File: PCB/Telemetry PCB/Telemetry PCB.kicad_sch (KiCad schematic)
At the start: 36 parts, among them IC1 E22-900M22S, J1 Conn_01x04_Pin, J2 GPS, J3 Batt, SW1 SW_MEC_5E, SW2 SW_MEC_5E, U1 STM32F411CEUx, U2 AP62200WU, Y1 25MHZ 9pF, Y2 32.768k 6pF

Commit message: added footprints
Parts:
- removed C15: 100-330nF, symbol Device:C
- removed L1: 1kohm 100MHz, symbol Device:L
- added C15: 1F, Capacitor_THT:C_Radial_D10.0mm_H20.0mm_P5.00mm, symbol Device:C_Polarized
- C1, C10, C11, C12, C13, C16, C17, C2, C3, C4, C5, C6, C7, C8, C9: footprint (none) -> Capacitor_SMD:C_1206_3216Metric_Pad1.33x1.80mm_HandSolder
- C14: value C -> 100nF; footprint (none) -> Capacitor_SMD:C_1206_3216Metric_Pad1.33x1.80mm_HandSolder
- J1, J2: footprint (none) -> Connector_PinHeader_2.54mm:PinHeader_1x04_P2.54mm_Vertical
- J3: footprint (none) -> Connector_PinHeader_2.54mm:PinHeader_1x02_P2.54mm_Vertical
- R1, R2, R3, R4, R5, R6: footprint (none) -> Resistor_SMD:R_1206_3216Metric_Pad1.30x1.75mm_HandSolder
- SW1, SW2: footprint (none) -> Button_Switch_SMD:SW_Push_1P1T_NO_6x6mm_H9.5mm
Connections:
- net +3.3V: now also C15.1
- net GND: now also C15.2
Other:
- note added: "Voltage Stabilization"

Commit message: more footprints
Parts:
- added J4: Serial Debug Header 1x4, Connector_PinHeader_2.54mm:PinHeader_1x04_P2.54mm_Vertical, symbol Connector_Generic:Conn_01x04
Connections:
- net +3.3V: now also J4.3 (Pin_3)
- net GND: now also J4.4 (Pin_4)
- net TX2: now reaches U1.12 (PA2)
- net TX2: now also J4.2 (Pin_2)
- net RX2: now reaches U1.13 (PA3)
- net RX2: now also J4.1 (Pin_1)
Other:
- note added: "Serial Debug Header"

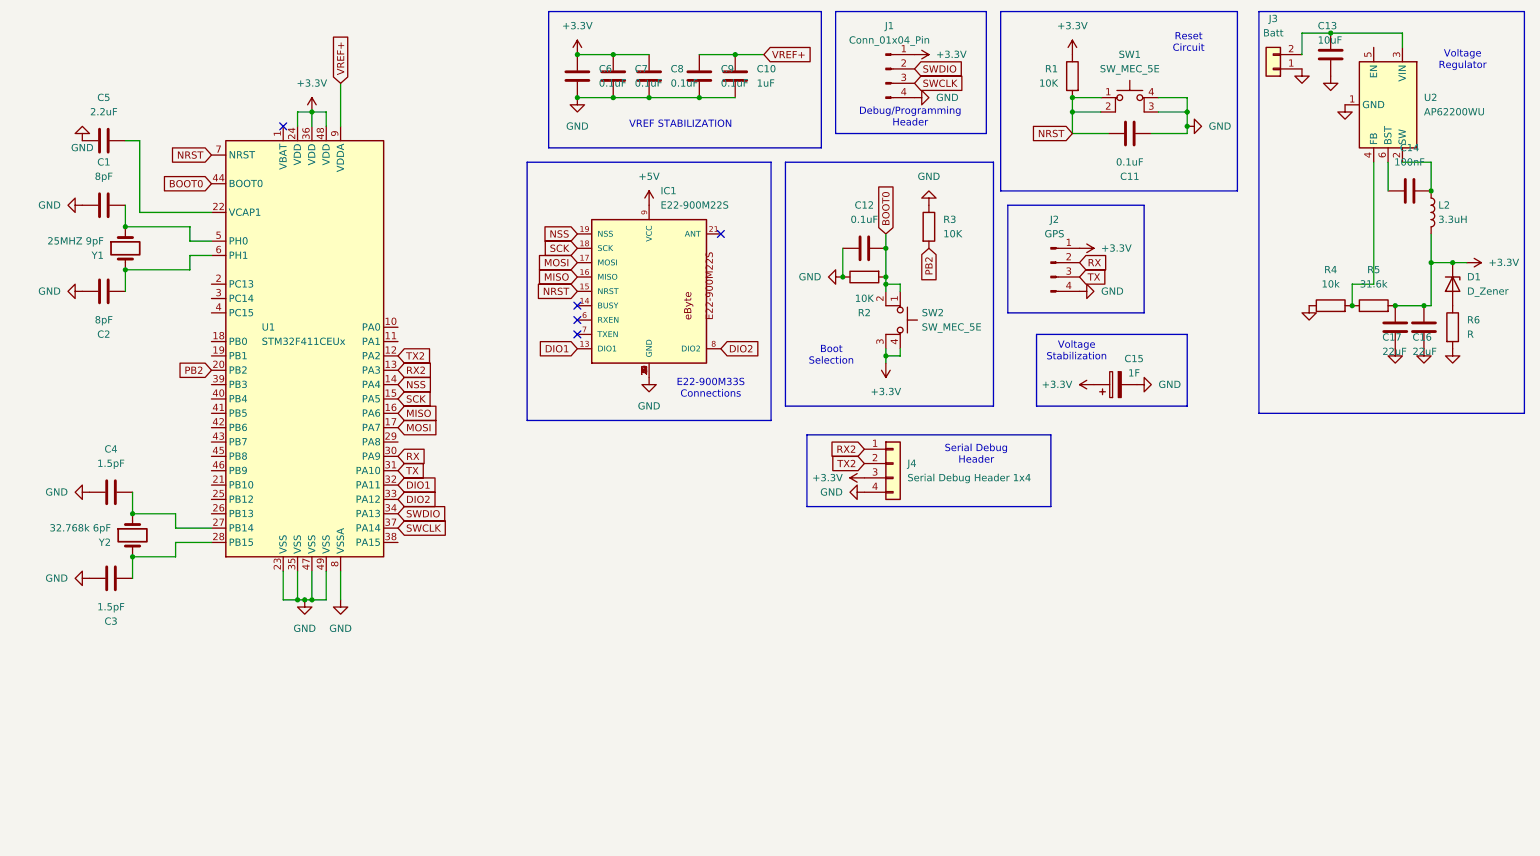
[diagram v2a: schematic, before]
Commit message: changed switching regulator to 5v added 3.3v linear regulator
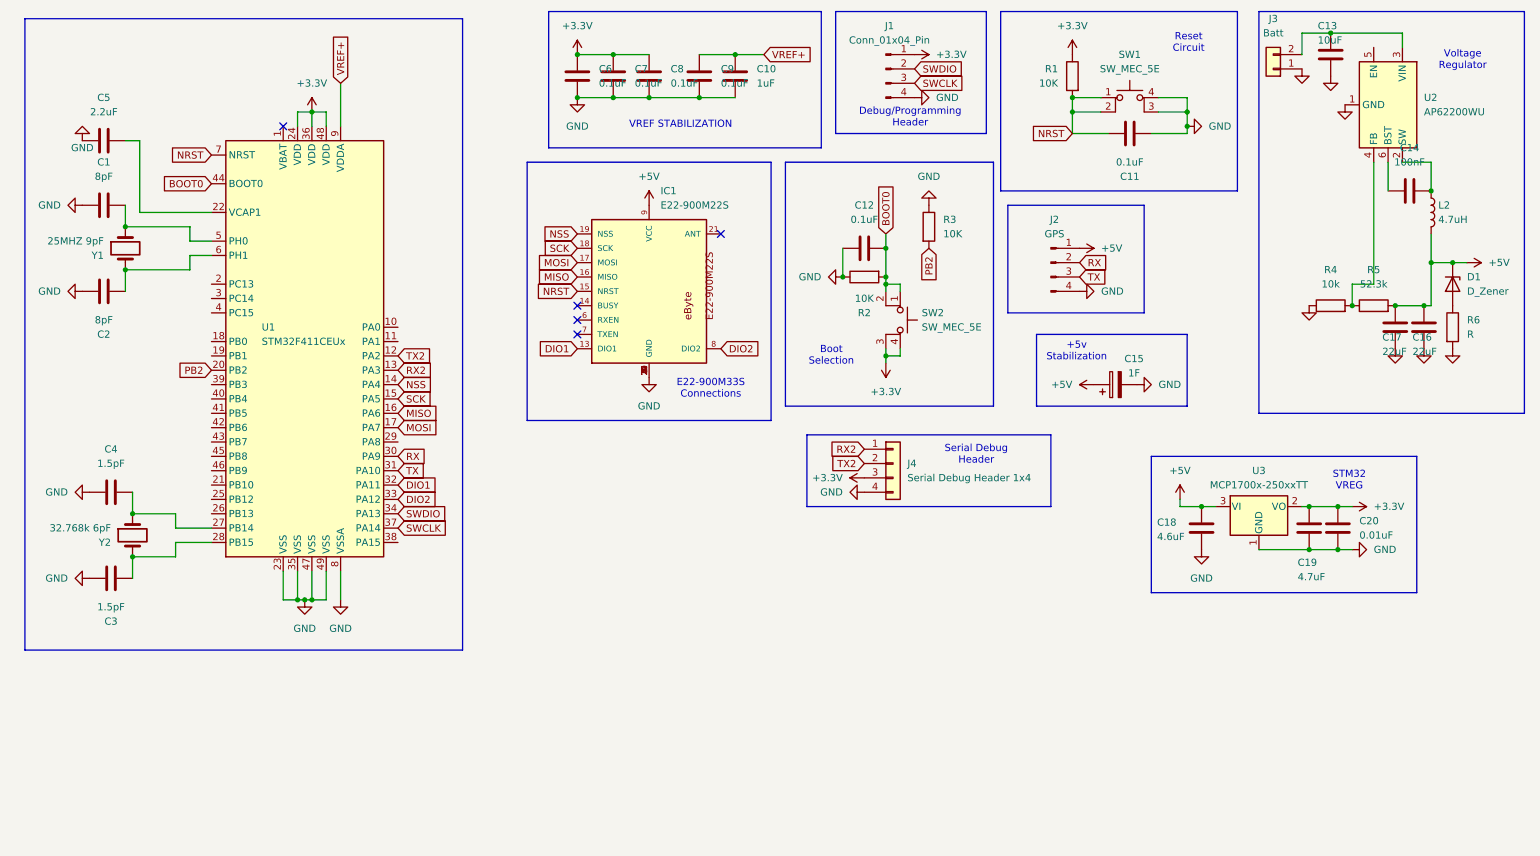
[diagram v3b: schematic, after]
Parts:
- added C18: 4.6uF, symbol Device:C
- added C19: 4.7uF, symbol Device:C
- added C20: 0.01uF, symbol Device:C
- added U3: MCP1700x-250xxTT, Package_TO_SOT_SMD:SOT-23, symbol Regulator_Linear:MCP1700x-250xxTT
- L2: value 3.3uH -> 4.7uH; footprint (none) -> SRN5040TA-220M:SRN5040TA-220M
- R5: value 31.6k -> 52.3k
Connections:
- net +3.3V: now also C19.1, C20.1, U3.2 (VO); no longer C15.1, C16.2, C17.2, D1.1 (K), J2.1 (Pin_1), L2.2, R5.2
- net +5V: now also C15.1, C16.2, C17.2, D1.1 (K), J2.1 (Pin_1), L2.2, R5.2, C18.1, U3.3 (VI)
- net GND: now also C18.2, C19.2, C20.2, U3.1 (GND)
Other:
- note added: "+5v Stabilization"
- note added: "STM32 VREG"
- note removed: "Voltage Stabilization"

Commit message: see last push discription
Last push did not work. see last push for description
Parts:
- removed SW1: SW_MEC_5E, Button_Switch_SMD:SW_Push_1P1T_NO_6x6mm_H9.5mm, symbol Switch:SW_MEC_5E
- added D2: 5.23V, PLZ5V1C_G3_H:CR_1C-G3&slash_H_VIS, symbol Device:D_Zener
- added J5: USB_C_Receptacle_USB2.0_16P, Connector_USB:USB_C_Receptacle_GCT_USB4105-xx-A_16P_TopMnt_Horizontal, symbol Connector:USB_C_Receptacle_USB2.0_16P
- added R7: 10, Capacitor_SMD:C_1206_3216Metric_Pad1.33x1.80mm_HandSolder, symbol Device:R
- added R8: 5.1k, Capacitor_SMD:C_1206_3216Metric_Pad1.33x1.80mm_HandSolder, symbol Device:R
- added SW2: SW_MEC_5E, Button_Switch_SMD:SW_Push_1P1T_NO_6x6mm_H9.5mm, symbol Switch:SW_MEC_5E
- C14: renamed from C18; footprint (none) -> Capacitor_SMD:C_1206_3216Metric_Pad1.33x1.80mm_HandSolder
- C15: renamed from C19; footprint (none) -> Capacitor_SMD:C_1206_3216Metric_Pad1.33x1.80mm_HandSolder
- C17: renamed from C20; footprint (none) -> Capacitor_SMD:C_1206_3216Metric_Pad1.33x1.80mm_HandSolder
- C2: renamed from C1; value 8pF -> 20pF
- C3: renamed from C2; value 8pF -> 20pF
- C4: value 1.5pF -> 5pF
- C5: renamed from C3; value 1.5pF -> 5pF
- D1: value D_Zener -> 5.23V; footprint (none) -> PLZ5V1C_G3_H:CR_1C-G3&slash_H_VIS
- L1: renamed from L2; footprint SRN5040TA-220M:SRN5040TA-220M -> SRN5040_3R3M:IND_SRN5040_BRN
- R6: value R -> 10; footprint Resistor_SMD:R_1206_3216Metric_Pad1.30x1.75mm_HandSolder -> Capacitor_SMD:C_1206_3216Metric_Pad1.33x1.80mm_HandSolder
- Y1: value 25MHZ 9pF -> 25MHZ 20pF; footprint (none) -> Crystal:Crystal_SMD_HC49-SD_HandSoldering
- Y2: value 32.768k 6pF -> 32.768k 12.5pF; footprint (none) -> ECS__327_12_5_34RR_TR:XTAL_ECS-.327-12.5-34RR-TR
- renumbered C5 to C1, C12 to C11, C15 to C12, C11 to C13, C13 to C16, C17 to C18, C14 to C19, C16 to C20, J4 to J2, J2 to J3, J3 to J4, R2 to R1, R3 to R2, R1 to R3, SW2 to SW1, U3 to U2, U2 to U3
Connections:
- net +3.3V: now also SW1.2 (K); no longer SW1.3 (K), SW1.4 (A)
- net +5V: now also D2.1 (K)
- net BOOT0: no longer SW1.2
- net DIO1: now also U1.45 (PB8); no longer U1.32 (PA11)
- net DIO2: now also U1.46 (PB9); no longer U1.33 (PA12)
- net GND: now also D1.2 (A), D2.2 (A), J5.A1 (GND), J5.A12 (GND), J5.B1 (GND), J5.B12 (GND), J5.S1 (SHIELD), R8.2, SW2.2 (K); no longer R6.2
- net NRST: now also SW2.1
- net at R6.1: now also U1.32 (PA11); no longer D1.2 (A)
- new net: R7.1, U1.33 (PA12)
- new net: J5.A5 (CC1), J5.B5 (CC2), R8.1
- new net USB +5V: J5.A4 (VBUS), J5.A9 (VBUS), J5.B4 (VBUS), J5.B9 (VBUS)
- new net USB Dn: J5.A7 (D-), J5.B7 (D-), R6.2
- new net USB Dp: J5.A6 (D+), J5.B6 (D+), R7.2
- no-connect marks 5 -> 8

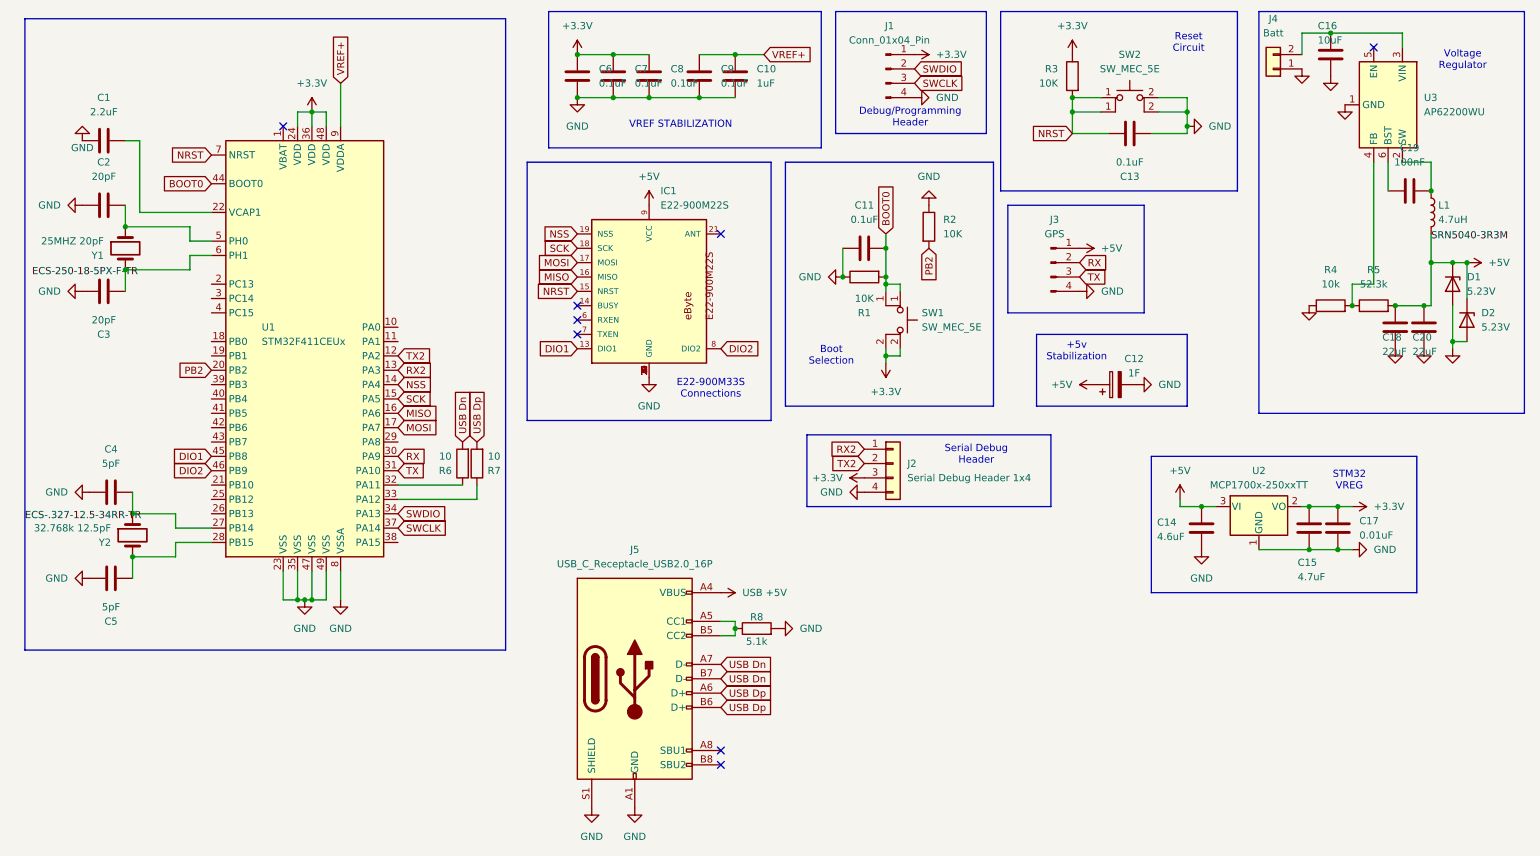
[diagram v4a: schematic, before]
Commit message: First Board Prototype
tweaked the filter caps for stm32. changed switches. and moved many pins around on the stm32 to ease trace routing. Created first board prototype
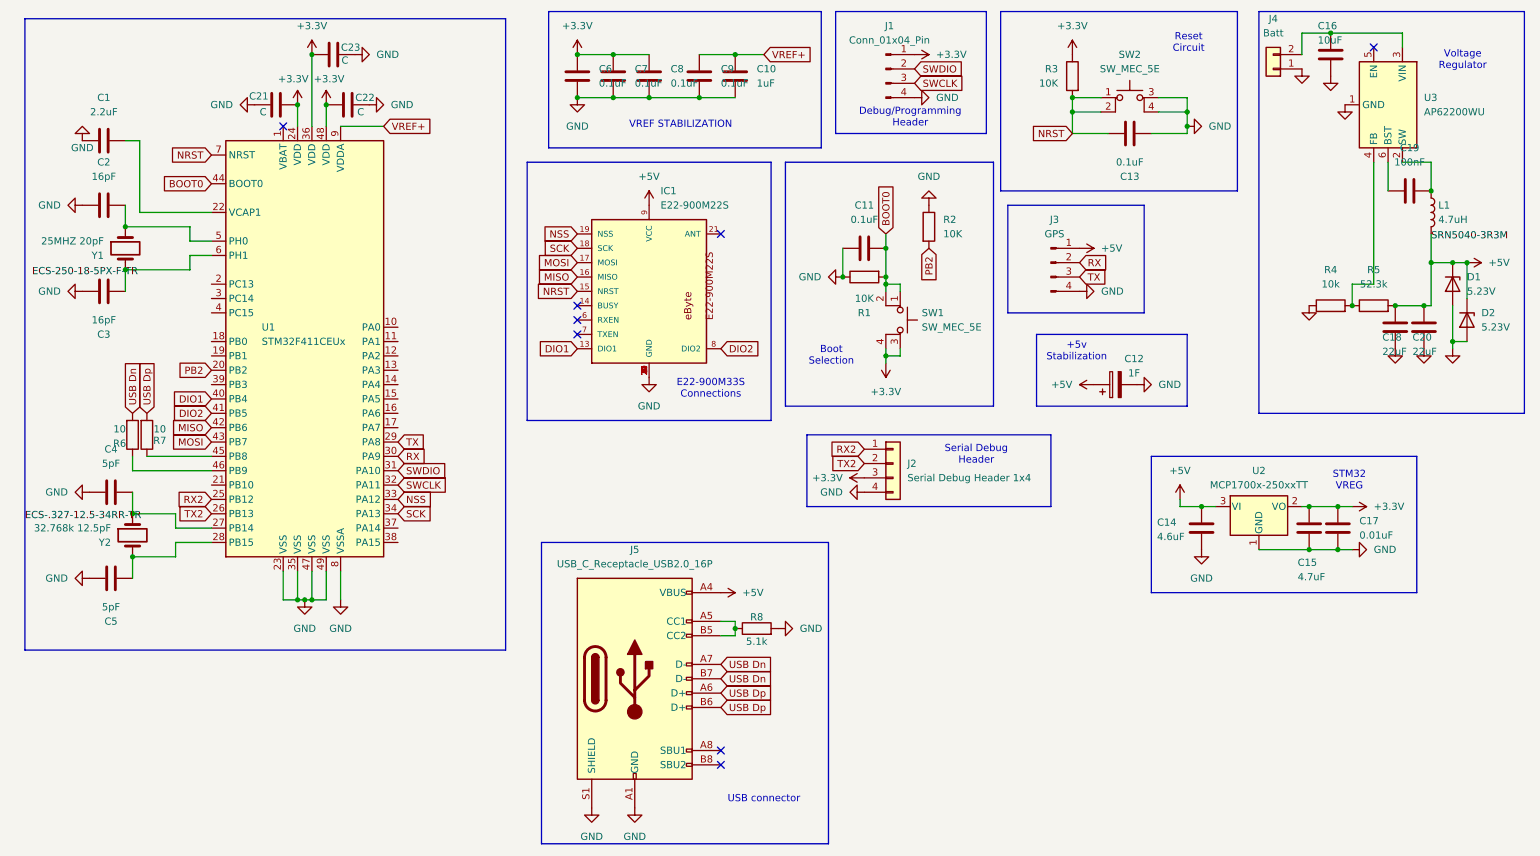
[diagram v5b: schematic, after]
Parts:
- added C21, C22, C23: C, Capacitor_SMD:C_1206_3216Metric_Pad1.33x1.80mm_HandSolder, symbol Device:C
- C2, C3: value 20pF -> 16pF
- SW1, SW2: footprint Button_Switch_SMD:SW_Push_1P1T_NO_6x6mm_H9.5mm -> PTS526_SM15_SMTR2_LFS:SON4_PTS526 SM15 SMTR2 LFS_CNK
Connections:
- net USB +5V is gone; now on net +5V: J5.A4 (VBUS), J5.A9 (VBUS), J5.B4 (VBUS), J5.B9 (VBUS)
- net +3.3V: now also SW1.3 (A), SW1.4 (K), C21.2, C22.1, C23.1; no longer SW1.2 (K)
- net BOOT0: now also SW1.2
- net DIO1: now also U1.40 (PB4); no longer U1.45 (PB8)
- net DIO2: now also U1.41 (PB5); no longer U1.46 (PB9)
- net GND: now also SW2.3 (A), SW2.4 (K), C21.1, C22.2, C23.2; no longer SW2.2 (K)
- net MISO: now also U1.42 (PB6); no longer U1.16 (PA6)
- net MOSI: now also U1.43 (PB7); no longer U1.17 (PA7)
- net NRST: now also SW2.2
- net NSS: now also U1.33 (PA12); no longer U1.14 (PA4)
- net RX2: now also U1.25 (PB12); no longer U1.13 (PA3)
- net SCK: now also U1.34 (PA13); no longer U1.15 (PA5)
- net SWCLK: now also U1.32 (PA11); no longer U1.37 (PA14)
- net SWDIO: now also U1.31 (PA10); no longer U1.34 (PA13)
- net TX: now also U1.29 (PA8); no longer U1.31 (PA10)
- net TX2: now also U1.26 (PB13); no longer U1.12 (PA2)
- net at R6.1: now also U1.46 (PB9); no longer U1.32 (PA11)
- net at R7.1: now also U1.45 (PB8); no longer U1.33 (PA12)
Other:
- note added: "USB connector"
- moved on the sheet: R6, R7

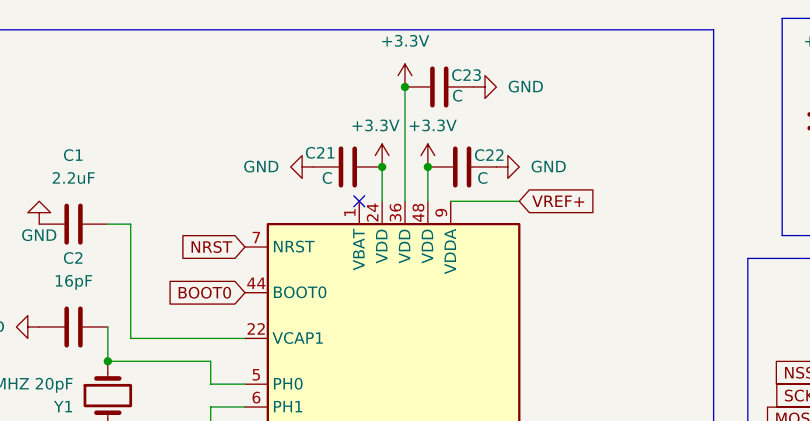
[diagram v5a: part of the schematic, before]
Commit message: Updated silkscreen and fixed front plane islands
Updated silkscreen and fixed front plane islands
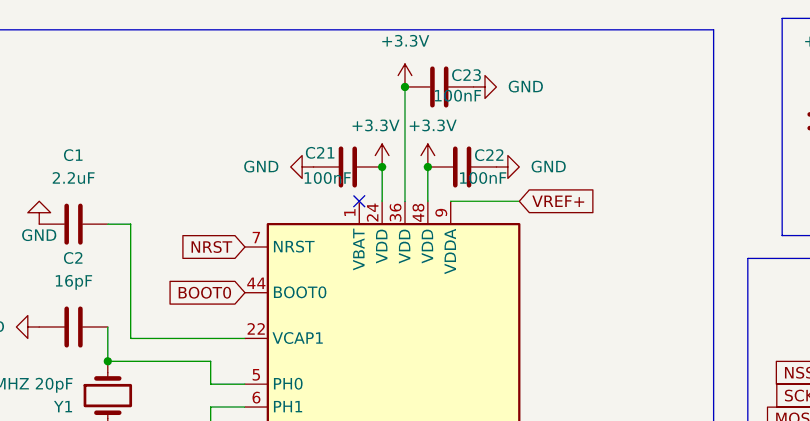
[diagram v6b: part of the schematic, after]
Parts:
- C21, C22, C23: value C -> 100nF
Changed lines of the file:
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@@
 			)
 		)
-		(property "Value" "C"
+		(property "Value" "100nF"
 			(at 73.152 23.876 90)
 			(effects
@@
 			)
 		)
-		(property "Value" "C"
+		(property "Value" "100nF"
 			(at 58.674 33.02 90)
 			(effects
@@
 			)
 		)
-		(property "Value" "C"
+		(property "Value" "100nF"
 			(at 75.946 33.02 90)
 			(effects
